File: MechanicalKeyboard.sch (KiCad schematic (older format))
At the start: 12 parts

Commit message: Update Reset Schematic
Finished designing the reset switch schematic
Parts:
- added R?: 10k, symbol Device:R_Small
- added SW?: SW_SKQG, symbol local:SW_SKQG
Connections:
- net +5V: now also R?.2
- net GND: now also SW?.2
- net RESET: now also R?.1, SW?.1
- no-connect marks 2 -> 4
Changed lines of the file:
@@
 Text GLabel 10000 1450 2    50   Input ~ 0
 MISO
+$Comp
+L local:SW_SKQG SW?
+U 1 1 60E51649
+P 7350 1250
+F 0 "SW?" H 7350 1575 50  0000 C CNN
+F 1 "SW_SKQG" H 7350 1484 50  0000 C CNN
+F 2 "" H 7350 1350 50  0001 C CNN
+F 3 "" H 7350 1350 50  0001 C CNN
+	1    7350 1250
+	1    0    0    -1
+$EndComp
+NoConn ~ 7600 1300
+NoConn ~ 7100 1150
+$Comp
+L power:GND #PWR?
+U 1 1 60E5374A
+P 7100 1300
+F 0 "#PWR?" H 7100 1050 50  0001 C CNN
+F 1 "GND" H 7105 1127 50  0000 C CNN
+F 2 "" H 7100 1300 50  0001 C CNN
+F 3 "" H 7100 1300 50  0001 C CNN
+	1    7100 1300
+	1    0    0    -1
+$EndComp
+$Comp
+L Device:R_Small R?
+U 1 1 60E54737
+P 7750 1050
+F 0 "R?" H 7650 950 50  0000 C CNN
+F 1 "10k" H 7650 1050 50  0000 C CNN
+F 2 "" H 7750 1050 50  0001 C CNN
+F 3 "~" H 7750 1050 50  0001 C CNN
+	1    7750 1050
+	-1   0    0    1
+$EndComp
+$Comp
+L power:+5V #PWR?
+U 1 1 60E56C02
+P 7750 950
+F 0 "#PWR?" H 7750 800 50  0001 C CNN
+F 1 "+5V" H 7765 1123 50  0000 C CNN
+F 2 "" H 7750 950 50  0001 C CNN
+F 3 "" H 7750 950 50  0001 C CNN
+	1    7750 950
+	1    0    0    -1
+$EndComp
+Text GLabel 7950 1150 2    50   Input ~ 0
+RESET
+Wire Wire Line
+	7600 1150 7750 1150
+Wire Wire Line
+	7750 1150 7950 1150
+Connection ~ 7750 1150
 $EndSCHEMATC

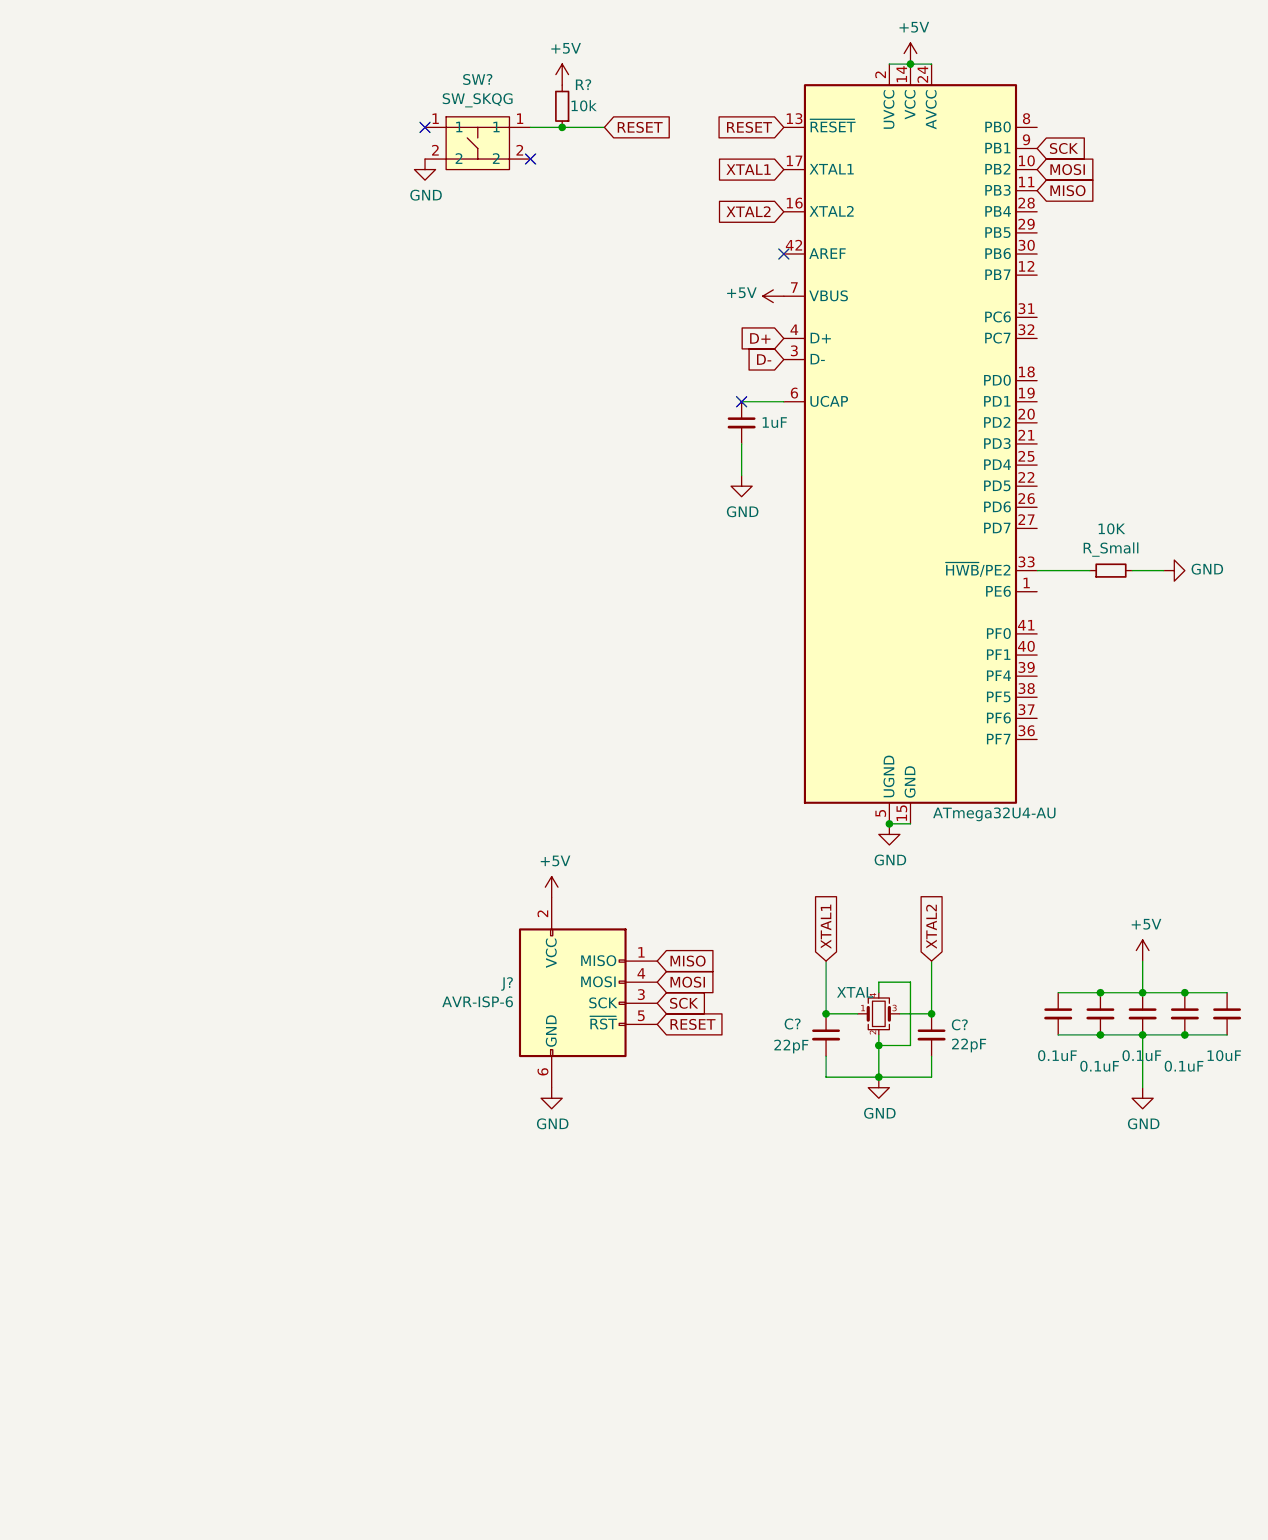
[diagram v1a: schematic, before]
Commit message: Update Schematic
adding circuit layouts for the USB-C implementation
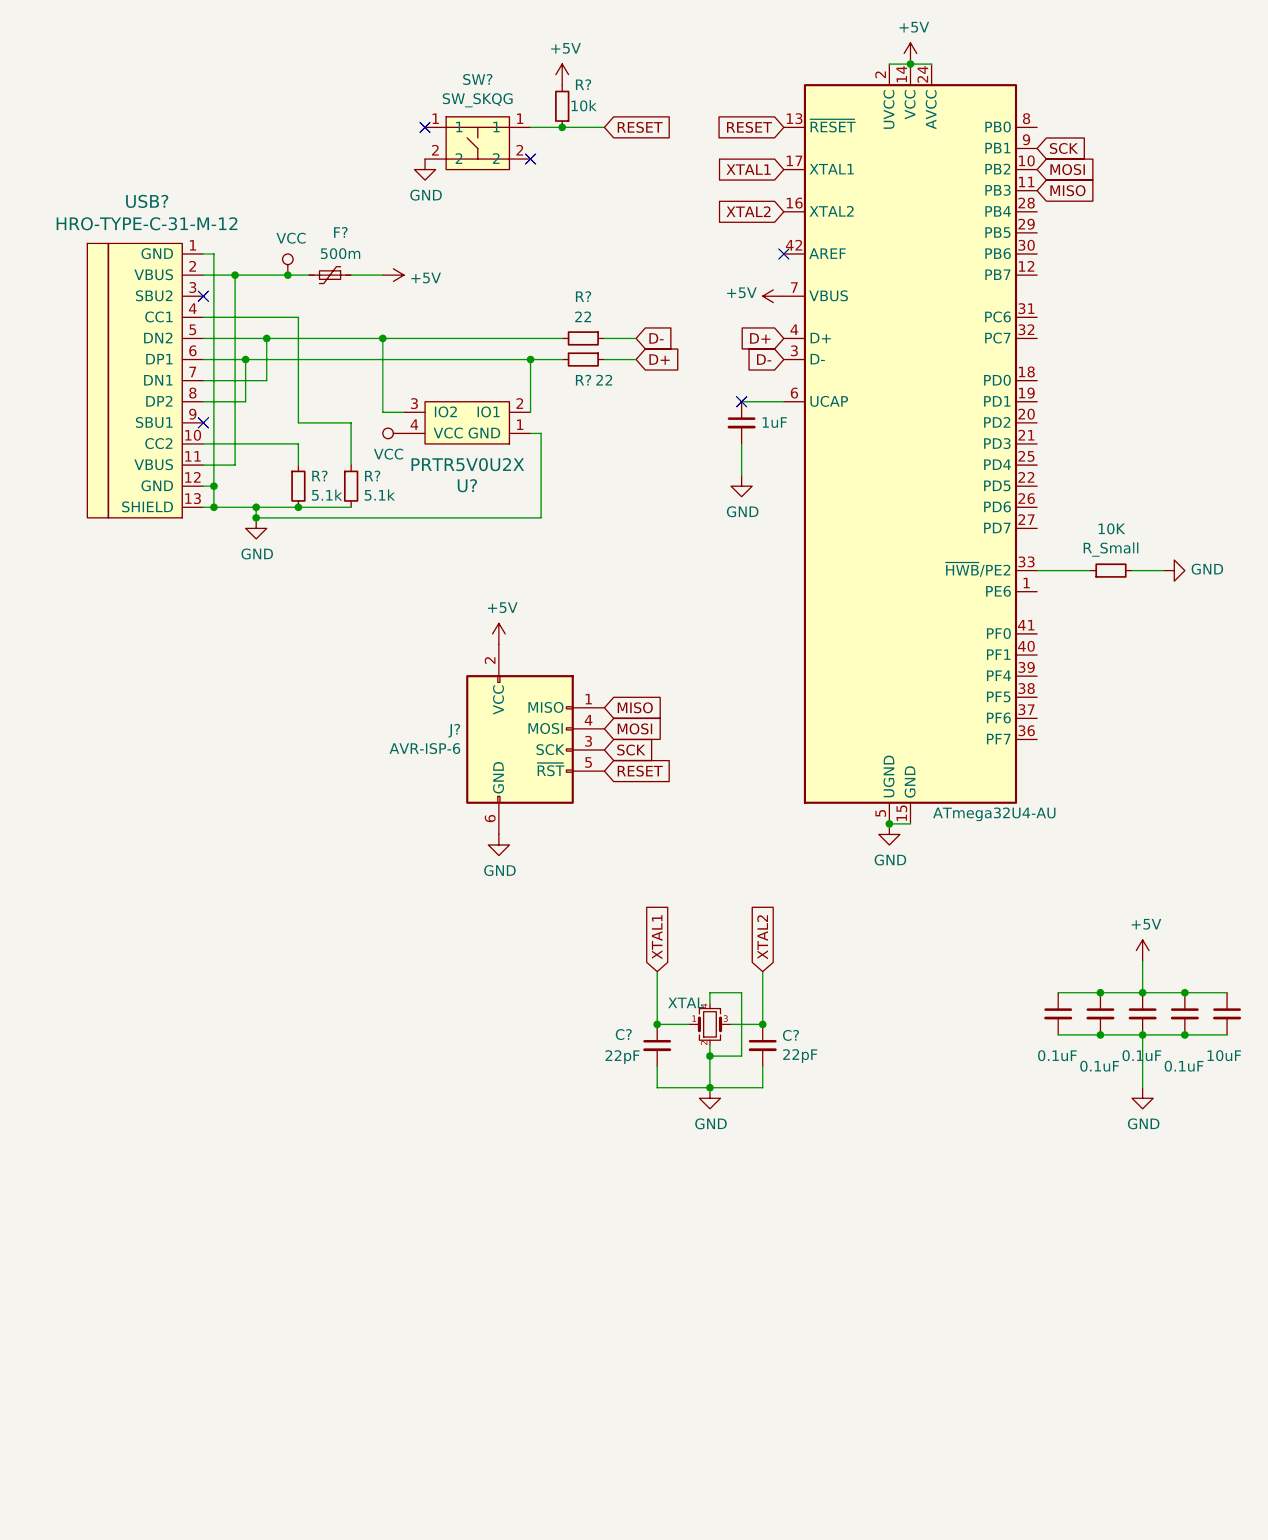
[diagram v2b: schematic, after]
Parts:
- added F?: 500m, symbol Device:Polyfuse_Small
- added R? (x2): 22, symbol Device:R_Small
- added R? (x2): 5.1k, symbol Device:R_Small
- added U?: PRTR5V0U2X, symbol random-keyboard-parts:PRTR5V0U2X
- added USB?: HRO-TYPE-C-31-M-12, symbol Type-C:HRO-TYPE-C-31-M-12
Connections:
- net +5V: now also F?.1
- net D+: now also R?.1
- net D-: now also R?.1
- net GND: now also R?.2, R?.2, U?.1 (GND), USB?.1 (GND), USB?.12 (GND), USB?.13 (SHIELD)
- new net: R?.1, USB?.10 (CC2)
- new net: R?.1, USB?.4 (CC1)
- new net: R?.2, U?.3 (IO2), USB?.5 (DN2), USB?.7 (DN1)
- new net: R?.2, U?.2 (IO1), USB?.6 (DP1), USB?.8 (DP2)
- new net VCC: F?.2, U?.4 (VCC), USB?.11 (VBUS), USB?.2 (VBUS)
- no-connect marks 4 -> 6
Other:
- moved on the sheet: C?, J?, XTAL

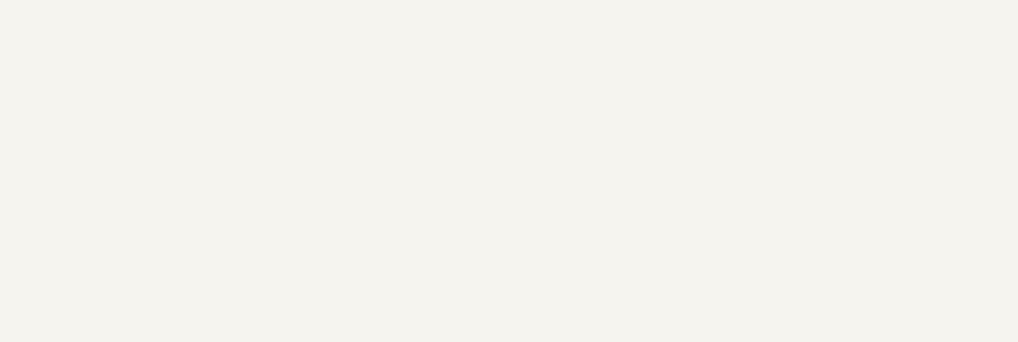
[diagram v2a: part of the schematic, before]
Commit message: Moved Schematic layout
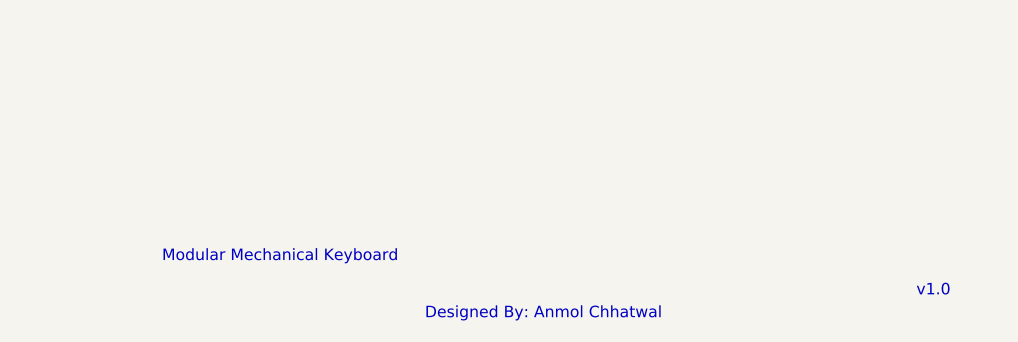
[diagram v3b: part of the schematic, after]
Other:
- note added: "Designed By: Anmol Chhatwal"
- note added: "Modular Mechanical Keyboard"
- note added: "v1.0"
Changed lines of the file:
@@
 Wire Wire Line
 	7600 2250 7750 2250
+Text Notes 7350 7500 0    50   ~ 0
+Modular Mechanical Keyboard
+Text Notes 10650 7650 0    50   ~ 0
+v1.0
+Text Notes 8500 7750 0    50   ~ 0
+Designed By: Anmol Chhatwal
 $EndSCHEMATC
